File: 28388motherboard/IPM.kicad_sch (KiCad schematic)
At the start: 26 parts, among them CN5 X3025WVS-2*10D-LPSW, Q37 SN74LVC1G125DCKR, Q39 SN74ACT244PWRG4, Q41 FMMT618TA

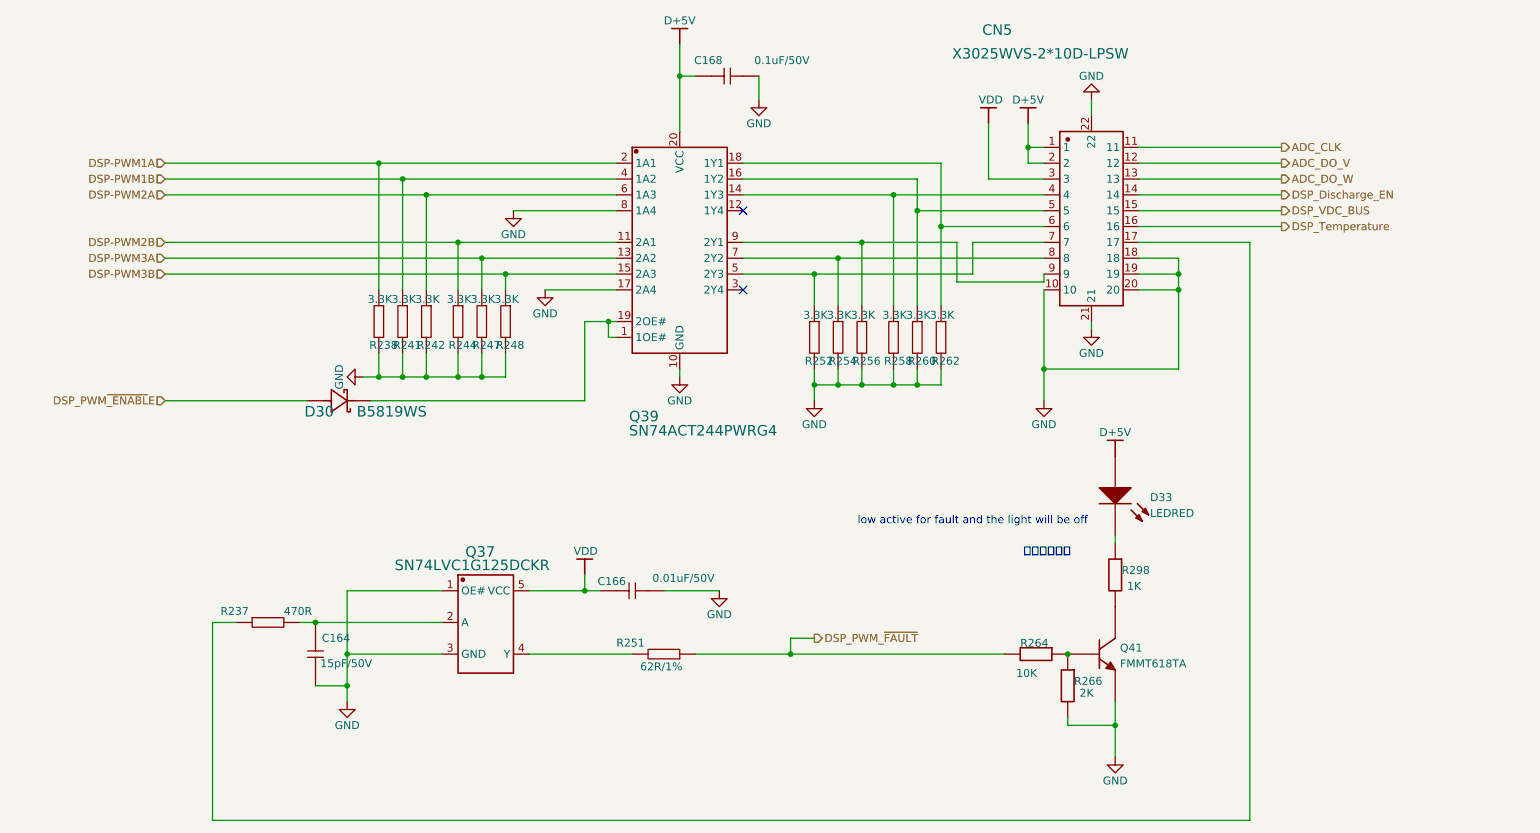
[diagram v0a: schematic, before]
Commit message: 底板分配引脚
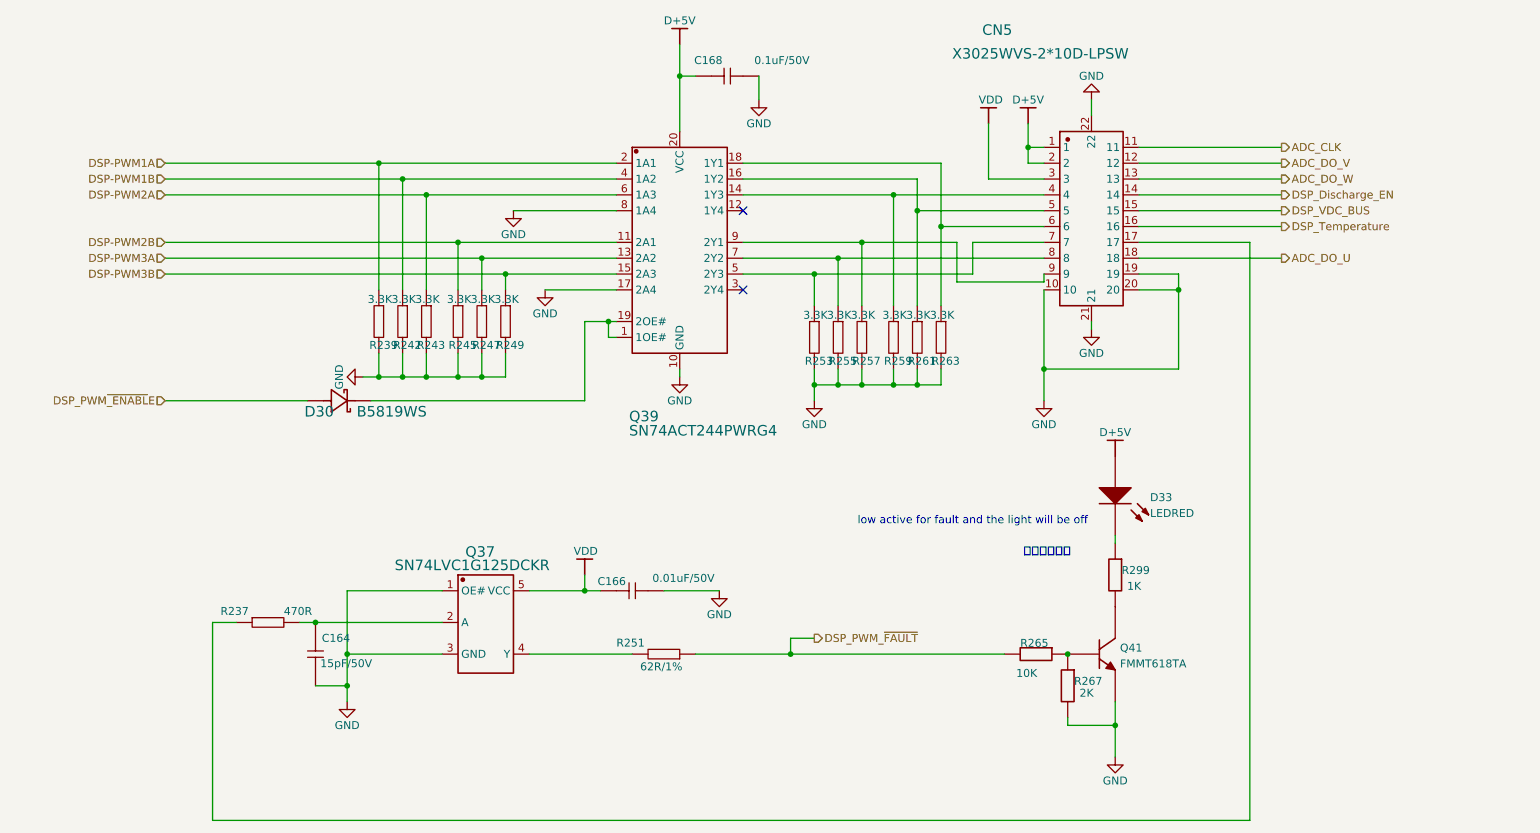
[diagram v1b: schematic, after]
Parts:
- renumbered R238 to R239, R241 to R242, R242 to R243, R244 to R245, R248 to R249, R252 to R253, R254 to R255, R256 to R257, R258 to R259, R260 to R261, R262 to R263, R264 to R265, R266 to R267, R298 to R299
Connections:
- net GND: no longer CN5.18
- new net ADC_DO_U: CN5.18

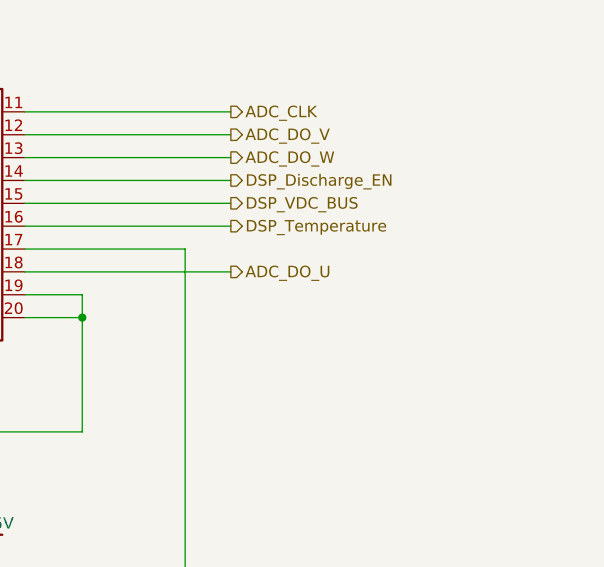
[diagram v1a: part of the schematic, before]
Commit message: 完成第一版引脚分配
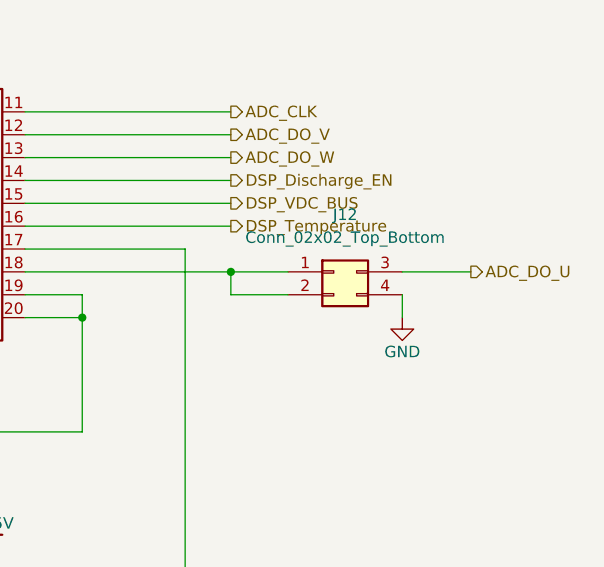
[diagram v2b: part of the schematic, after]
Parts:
- added J12: Conn_02x02_Top_Bottom, symbol Connector_Generic:Conn_02x02_Top_Bottom
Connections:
- net ADC_DO_U: now also J12.3 (Pin_3); no longer CN5.18
- net GND: now also J12.4 (Pin_4)
- new net: CN5.18, J12.1 (Pin_1), J12.2 (Pin_2)
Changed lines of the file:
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@@
 	)
 	(junction
+		(at 223.52 67.31)
+		(diameter 0)
+		(color 0 0 0 0)
+	)
+	(junction
 		(at 95.25 86.36)
 		(diameter 0)
@@
 	(wire
 		(pts
-			(xy 200.66 67.31) (xy 223.52 67.31)
-		)
-		(stroke
-			(width 0)
-			(type default)
-		)
-	)
-	(wire
-		(pts
 			(xy 78.74 86.36) (xy 78.74 82.55)
 		)
@@
 	(wire
 		(pts
+			(xy 223.52 69.85) (xy 223.52 67.31)
+		)
+		(stroke
+			(width 0)
+			(type default)
+		)
+	)
+	(wire
+		(pts
 			(xy 156.21 85.09) (xy 156.21 87.63)
 		)
@@
 	(wire
 		(pts
+			(xy 242.57 69.85) (xy 242.57 72.39)
+		)
+		(stroke
+			(width 0)
+			(type default)
+		)
+	)
+	(wire
+		(pts
 			(xy 111.76 77.47) (xy 111.76 90.17)
 		)
@@
 	(wire
 		(pts
+			(xy 229.87 69.85) (xy 223.52 69.85)
+		)
+		(stroke
+			(width 0)
+			(type default)
+		)
+	)
+	(wire
+		(pts
+			(xy 200.66 67.31) (xy 223.52 67.31)
+		)
+		(stroke
+			(width 0)
+			(type default)
+		)
+	)
+	(wire
+		(pts
 			(xy 207.01 69.85) (xy 200.66 69.85)
 		)
@@
 	(wire
 		(pts
+			(xy 223.52 67.31) (xy 229.87 67.31)
+		)
+		(stroke
+			(width 0)
+			(type default)
+		)
+	)
+	(wire
+		(pts
 			(xy 95.25 86.36) (xy 95.25 82.55)
 		)
@@
 	(wire
 		(pts
+			(xy 242.57 67.31) (xy 250.19 67.31)
+		)
+		(stroke
+			(width 0)
+			(type default)
+		)
+	)
+	(wire
+		(pts
 			(xy 116.84 57.15) (xy 86.36 57.15)
 		)
@@
 	(hierarchical_label "ADC_DO_U"
 		(shape output)
-		(at 223.52 67.31 0)
+		(at 250.19 67.31 0)
 		(effects
 			(font
@@
 					(unit 1)
 				)
+			)
+		)
+	)
+	(symbol
+		(lib_id "Connector_Generic:Conn_02x02_Top_Bottom")
+		(at 234.95 67.31 0)
+		(unit 1)
+		(exclude_from_sim no)
+		(in_bom yes)
+		(on_board yes)
+		(dnp no)
+		(fields_autoplaced yes)
+		(property "Reference" "J12"
+			(at 236.22 60.96 0)
+			(effects
+				(font
+					(size 1.27 1.27)
+				)
+			)
+		)
+		(property "Value" "Conn_02x02_Top_Bottom"
+			(at 236.22 63.5 0)
+			(effects
+				(font
+					(size 1.27 1.27)
+				)
+			)
+		)
+		(property "Footprint" ""
+			(at 234.95 67.31 0)
+			(effects
+				(font
+					(size 1.27 1.27)
+				)
+				(hide yes)
+			)
+		)
+		(property "Datasheet" "~"
+			(at 234.95 67.31 0)
+			(effects
+				(font
+					(size 1.27 1.27)
+				)
+				(hide yes)
+			)
+		)
+		(property "Description" "Generic connector, double row, 02x02, top/bottom pin numbering scheme (row 1: 1...pins_per_row, row2: pins_per_row+1 ... num_pins), script generated (kicad-library-utils/schlib/autogen/connector/)"
+			(at 234.95 67.31 0)
+			(effects
+				(font
+					(size 1.27 1.27)
+				)
+				(hide yes)
+			)
+		)
+		(pin "3"
+		)
+		(pin "2"
+		)
+		(pin "1"
+		)
+		(pin "4"
+		)
+		(instances
+			(project ""
+				(path "/88c87a56-bf0e-49aa-812f-d0846700c8ff/b36735eb-d769-4ff2-afa1-3dc92bc587d0"
+					(reference "J12")
+					(unit 1)
+				)
+				(path "/88c87a56-bf0e-49aa-812f-d0846700c8ff/d4aa48ef-e51b-4c23-93aa-156d0b4235e3"
+					(reference "J13")
+					(unit 1)
+				)
+			)
+		)
+	)
+	(symbol
+		(lib_id "power:GND")
+		(at 242.57 72.39 0)
+		(unit 1)
+		(exclude_from_sim no)
+		(in_bom yes)
+		(on_board yes)
+		(dnp no)
+		(property "Reference" "#PWR0481"
+			(at 242.57 78.74 0)
+			(effects
+				(font
+					(size 1.27 1.27)
+				)
+				(hide yes)
+			)
+		)
+		(property "Value" "GND"
+			(at 242.57 76.2 0)
+			(effects
+				(font
+					(size 1.27 1.27)
+				)
+			)
+		)
+		(property "Footprint" ""
+			(at 242.57 72.39 0)
+			(effects
+				(font
+					(size 1.27 1.27)
+				)
+				(hide yes)
+			)
+		)
+		(property "Datasheet" ""
+			(at 242.57 72.39 0)
+			(effects
+				(font
+					(size 1.27 1.27)
+				)
+				(hide yes)
+			)
+		)
+		(property "Description" "Power symbol creates a global label with name \"GND\" , ground"
+			(at 242.57 72.39 0)
+			(effects
+				(font
+					(size 1.27 1.27)
+				)
+				(hide yes)
+			)
+		)
+		(pin "1"
+		)
+		(instances
+			(project "28388motherboard"
+				(path "/88c87a56-bf0e-49aa-812f-d0846700c8ff/b36735eb-d769-4ff2-afa1-3dc92bc587d0"
+					(reference "#PWR0481")
+					(unit 1)
+				)
+				(path "/88c87a56-bf0e-49aa-812f-d0846700c8ff/d4aa48ef-e51b-4c23-93aa-156d0b4235e3"
+					(reference "#PWR0482")
+					(unit 1)
+				)

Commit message: 修改了一些bug，进行了一些布线
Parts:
- J17: renamed from J12; footprint (none) -> Connector_PinHeader_2.54mm:PinHeader_2x02_P2.54mm_Vertical_SMD
- renumbered C164 to C39, C166 to C40, C168 to C41, D30 to D16, D33 to D17, Q37 to Q14, Q39 to Q15, Q41 to Q16, R237 to R54, R239 to R55, R242 to R56, R243 to R57, R245 to R58, R247 to R59, R249 to R60, R251 to R61, R253 to R62, R255 to R63, R257 to R64, R259 to R65, R261 to R66, R263 to R67, R265 to R68, R267 to R69, R299 to R70

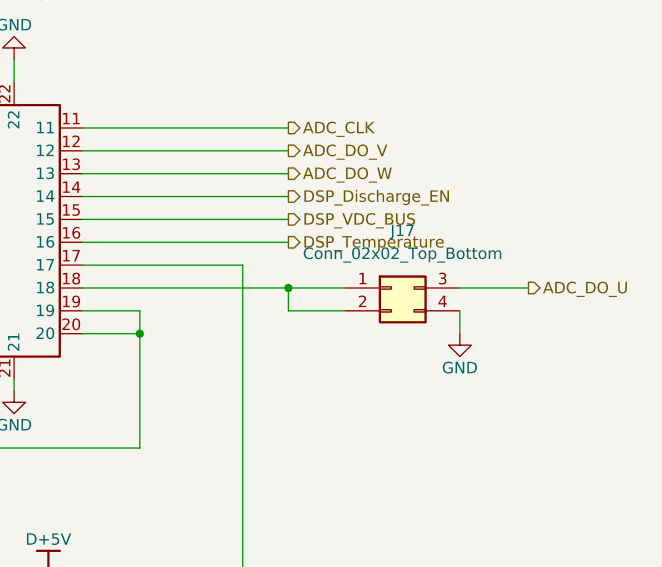
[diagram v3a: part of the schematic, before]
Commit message: 基本完成初步的布线，但是额外逆变器接口位置极不合理，需要返工
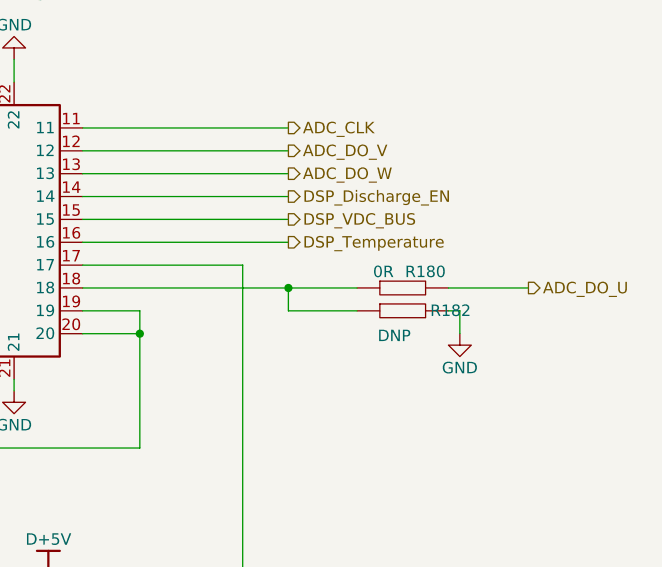
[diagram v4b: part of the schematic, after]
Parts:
- removed J17: Conn_02x02_Top_Bottom, Connector_PinHeader_2.54mm:PinHeader_2x02_P2.54mm_Vertical_SMD, symbol Connector_Generic:Conn_02x02_Top_Bottom
- added R180: 0R, Lib_sheet_10:R_0603_1608Metric, symbol sheet1-altium-import:RES_2
- added R182: DNP, Lib_sheet_10:R_0603_1608Metric, symbol sheet1-altium-import:RES_2
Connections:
- net ADC_DO_U: now also R180.2
- net GND: now also R182.2
- net at CN5.18: now also R180.1, R182.1
